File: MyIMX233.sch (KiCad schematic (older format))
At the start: 40 parts, among them IC1 iMX233, IC2 DDR_SDRAM_MT46_x16, J1 USB_A, J2 Micro_SD_Card, SW1 SWITCH_PUSHBUTTON, Y1 24Mhz

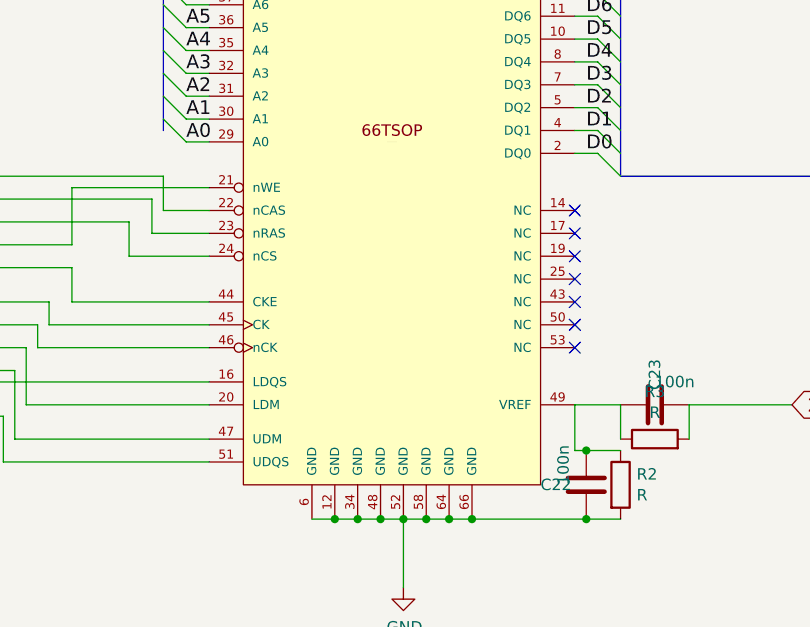
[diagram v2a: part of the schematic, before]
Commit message: refs added plus tuned lengths of d8..15 and addr
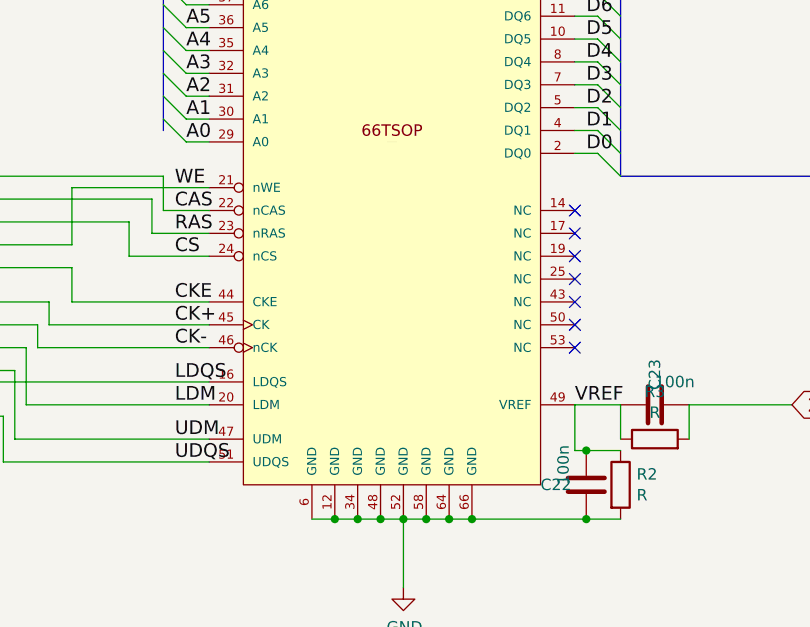
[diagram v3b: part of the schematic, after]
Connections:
- net CK+: now reaches IC1.36 (EMI_CLK), IC2.45 (CK)
- net CK-: now reaches IC1.37 (EMI_CLKn), IC2.46 (nCK)
- net LDQS: now reaches IC1.39 (EMI_DQS0), IC2.16 (LDQS)
- net UDQS: now reaches IC1.40 (EMI_DQS1), IC2.51 (UDQS)
- net LDM: now reaches IC1.46 (EMI_DQM0), IC2.20 (LDM)
- net UDM: now reaches IC1.56 (EMI_DQM1), IC2.47 (UDM)
- net CAS: now reaches IC1.61 (EMI_CASn), IC2.22 (nCAS)
- net RAS: now reaches IC1.62 (EMI_RASn), IC2.23 (nRAS)
- net CS: now reaches IC1.63 (EMI_CE0n), IC2.24 (nCS)
- net WE: now reaches IC1.77 (EMI_WEn), IC2.21 (nWE)
- net CKE: now reaches IC1.78 (EMI_CKE), IC2.44 (CKE)
- net VREF: now reaches C22.2, C23.1, IC2.49 (VREF), R2.1, R3.1
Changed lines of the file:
@@
 Wire Wire Line
 	2800 6800 2500 6800
+Text Label 10550 5550 0    60   ~ 0
+VREF
+Text Label 8800 4600 0    60   ~ 0
+WE
+Text Label 8800 4700 0    60   ~ 0
+CAS
+Text Label 8800 4800 0    60   ~ 0
+RAS
+Text Label 8800 4900 0    60   ~ 0
+CS
+Text Label 8800 5100 0    60   ~ 0
+CKE
+Text Label 8800 5200 0    60   ~ 0
+CK+
+Text Label 8800 5300 0    60   ~ 0
+CK-
+Text Label 8800 5450 0    60   ~ 0
+LDQS
+Text Label 8800 5550 0    60   ~ 0
+LDM
+Text Label 8800 5700 0    60   ~ 0
+UDM
+Text Label 8800 5800 0    60   ~ 0
+UDQS
 $EndSCHEMATC

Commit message: updated pcb export with 3d step files plus my new DDR step and FreeCAD proj
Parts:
- J1: footprint Connectors:USB_Micro-B -> mylib:USB_Micro-B_MOLEX_105017-0001
- J2: footprint Connectors_Hirose:microSD_Card_Receptacle_Hirose_DM3AT-SF-PEJM5 -> mylib:microSD_Card_Receptacle_Hirose_DM3AT-SF-PEJM5
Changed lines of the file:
@@
 F 0 "J1" H 1805 4117 50  0000 C CNN
 F 1 "USB_A" H 1805 4026 50  0000 C CNN
-F 2 "Connectors:USB_Micro-B" H 1900 3600 50  0001 C CNN
+F 2 "mylib:USB_Micro-B_MOLEX_105017-0001" H 1900 3600 50  0001 C CNN
 F 3 "" H 1900 3600 50  0001 C CNN
 	1    1750 3650
@@
 F 0 "J2" H 1700 9217 50  0000 C CNN
 F 1 "Micro_SD_Card" H 1700 9126 50  0000 C CNN
-F 2 "Connectors_Hirose:microSD_Card_Receptacle_Hirose_DM3AT-SF-PEJM5" H 2900 8800 50  0001 C CNN
+F 2 "mylib:microSD_Card_Receptacle_Hirose_DM3AT-SF-PEJM5" H 2900 8800 50  0001 C CNN
 F 3 "" H 1750 8500 50  0001 C CNN
 	1    1750 8500

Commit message: before dcdc
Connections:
- net SD_CMD: now reaches IC1.83 (SSP1_CMD-JTAG_TDO), J2.3 (CMD)
- net SD0: now reaches IC1.84 (SSP1_DATA0-JTAG_TDI), J2.7 (DAT0)
- net SD1: now reaches IC1.85 (SSP1_DATA1-I2C_SCL-JTAG_TCLK), J2.8 (DAT1)
- net SD2: now reaches IC1.86 (SSP1_DATA2-I2C_SDA-JTAG_RTCK), J2.1 (DAT2)
- net SD3: now reaches IC1.87 (SSP1_DATA3-JTAG_TMS), J2.2 (DAT3/CD)
- net SD_CLK: now reaches IC1.90 (SSP1_SCK-JTAG_TRST), J2.5 (CLK)
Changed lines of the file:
@@
 	2950 8200 2650 8200
-Wire Wire Line
-	3250 8400 3250 8450
-Wire Wire Line
-	3250 8450 2800 8450
-Wire Wire Line
-	2800 8450 2800 8300
 Wire Wire Line
 	2800 8300 2650 8300
@@
 Text Label 8800 5800 0    60   ~ 0
 UDQS
+Wire Wire Line
+	3250 8425 2800 8425
+Wire Wire Line
+	2800 8425 2800 8300
+Wire Wire Line
+	3250 8425 3250 8400
+Text Label 3125 8100 0    60   ~ 0
+SD0
+Text Label 3150 8200 0    60   ~ 0
+SD1
+Text Label 2675 8200 0    60   ~ 0
+SD2
+Text Label 3175 8425 0    60   ~ 0
+SD3
+Text Label 3100 8600 0    60   ~ 0
+SD_CLK
+Text Label 3175 8000 0    60   ~ 0
+SD_CMD
 $EndSCHEMATC

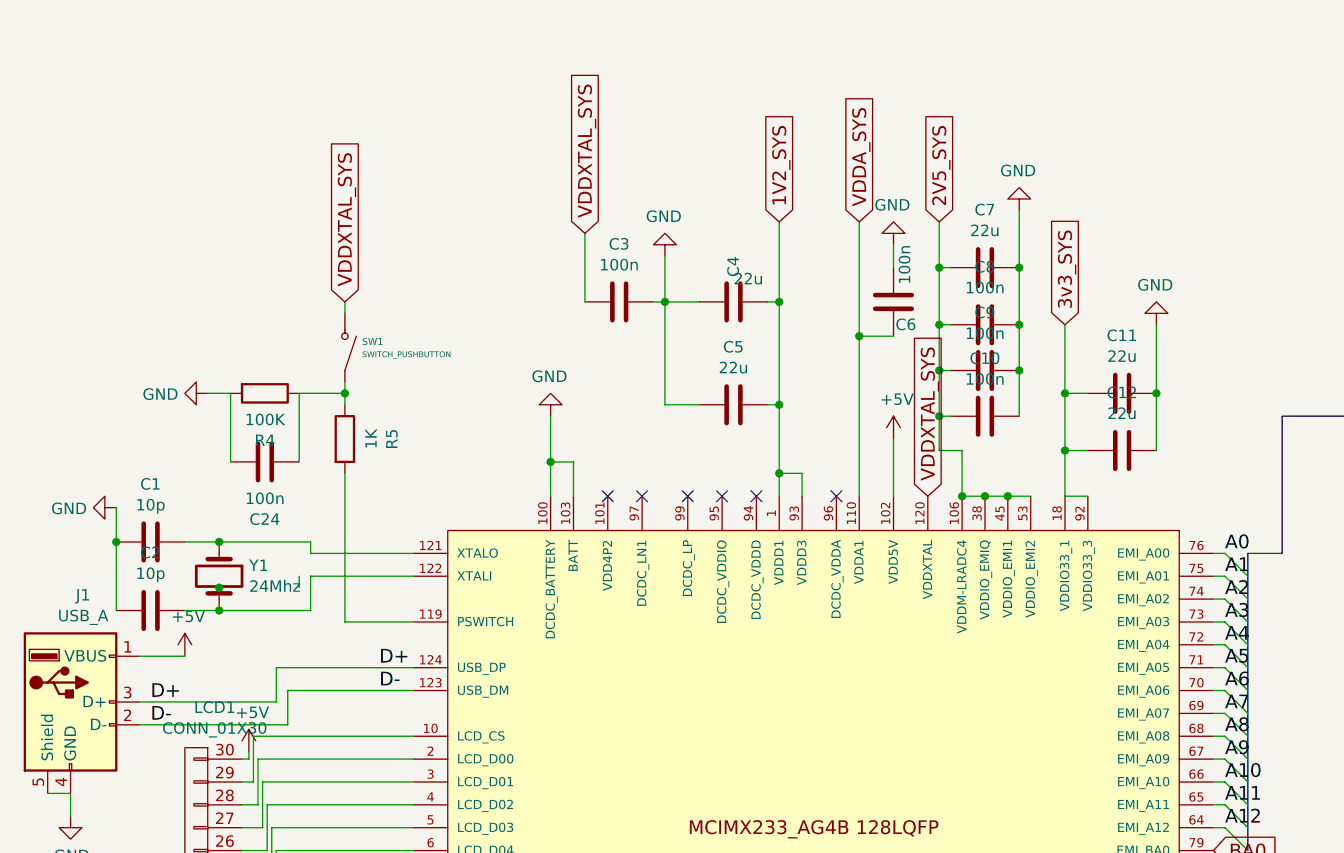
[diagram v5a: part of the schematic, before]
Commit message: updated with step files new battery and inductor diag
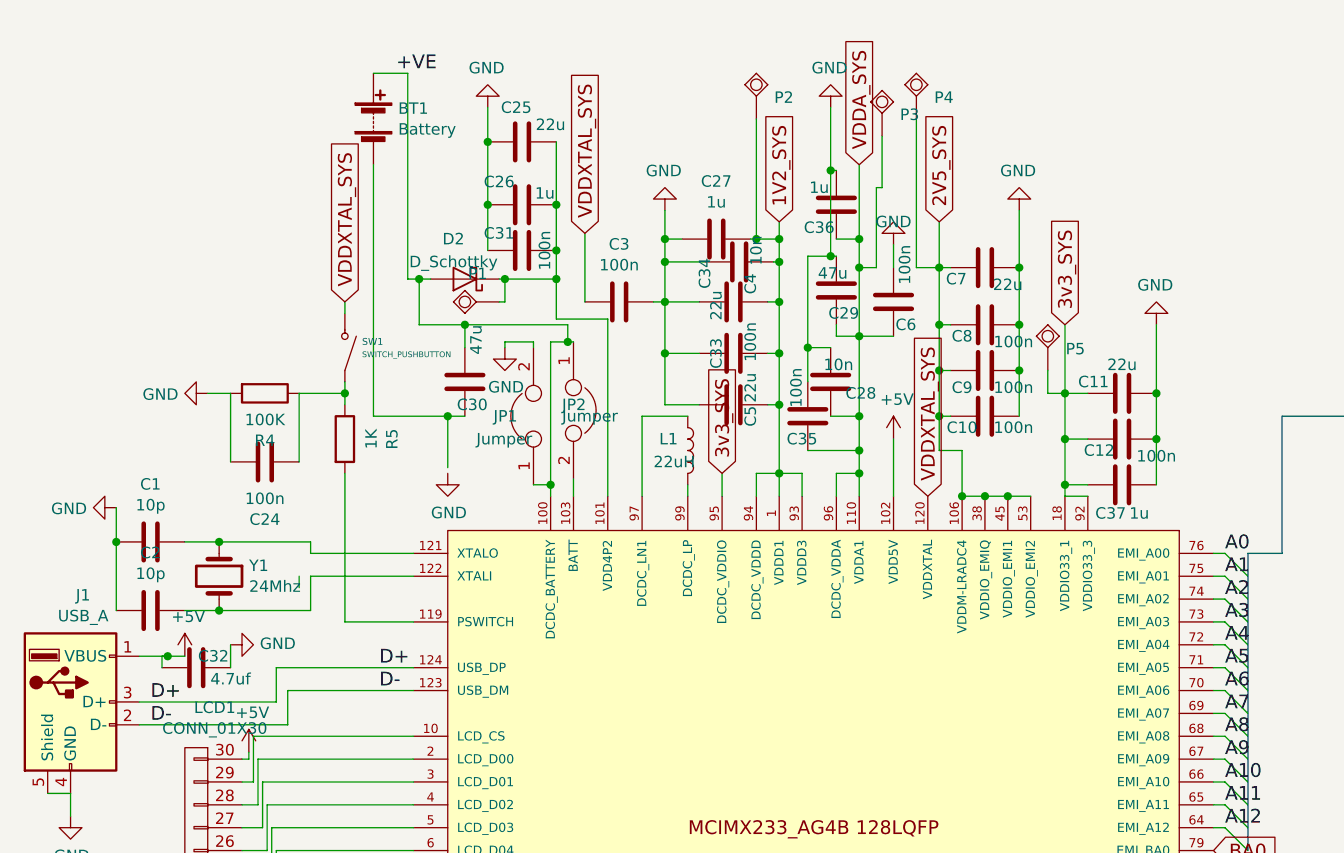
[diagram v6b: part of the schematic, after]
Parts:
- added BT1: Battery, Connectors_JST:JST_XH_B02B-XH-A_02x2.50mm_Straight, symbol Battery
- added C25: 22u, Capacitors_SMD:C_0805_HandSoldering, symbol C
- added C26, C27: 1u, Capacitors_SMD:C_0402, symbol C
- added C28, C34: 10n, Capacitors_SMD:C_0402, symbol C
- added C29, C30: 47u, Capacitors_SMD:C_0805_HandSoldering, symbol C
- added C31, C33, C35: 100n, Capacitors_SMD:C_0402, symbol C
- added C32: 4.7uf, Capacitors_SMD:C_0603_HandSoldering, symbol C
- added C36, C37: 1u, Capacitors_SMD:C_0603_HandSoldering, symbol C
- added D2: D_Schottky, Diodes_SMD:D_SOD-323_HandSoldering, symbol D_Schottky
- added JP1, JP2: Jumper, Pin_Headers:Pin_Header_Straight_1x02_Pitch2.54mm, symbol Jumper
- added L1: 22uH, mylib:Bourns22uh6x6mm, symbol L
- added P1: P4v2, iMX233-OLinuXino-NANO_Rev_B:GOGO_TESTPAD40_OBLONG, symbol GOGO_TESTPAD
- added P2: 1v2, iMX233-OLinuXino-NANO_Rev_B:GOGO_TESTPAD40_OBLONG, symbol GOGO_TESTPAD
- added P3: VDDA1v8, iMX233-OLinuXino-NANO_Rev_B:GOGO_TESTPAD40_OBLONG, symbol GOGO_TESTPAD
- added P4: 2v5, iMX233-OLinuXino-NANO_Rev_B:GOGO_TESTPAD40_OBLONG, symbol GOGO_TESTPAD
- added P5: 3v3, iMX233-OLinuXino-NANO_Rev_B:GOGO_TESTPAD40_OBLONG, symbol GOGO_TESTPAD
- C12: value 22u -> 100n
- C13: footprint Capacitors_SMD:C_0603 -> Capacitors_SMD:C_0603_HandSoldering
- IC2: footprint opendous:TSOP66_JEDEC_DDR_SDRAM -> mylib:TSOP66_JEDEC_DDR_SDRAM
- J1: footprint mylib:USB_Micro-B_MOLEX_105017-0001 -> conn-fci:CONN-10118194-0001LF-FCI
- R1, R4, R5: footprint Resistors_SMD:R_0603 -> Resistors_SMD:R_0603_HandSoldering
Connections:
- net +5V: now also C32.1
- net 1V2_SYS: now also IC1.94 (DCDC_VDDD), C27.2, C33.1, C34.1, P2.P$1 (PP)
- net 2V5_SYS: now also P4.P$1 (PP)
- net 3v3_SYS: now also IC1.95 (DCDC_VDDIO), C37.1, P5.P$1 (PP)
- net GND: now also C25.1, C26.1, C27.1, C28.1, C29.1, C31.2, C32.2, C33.2, C34.2, C35.1, C36.1, C37.2, JP1.2; no longer IC1.100 (DCDC_BATTERY), IC1.103 (BATT)
- net VDDA_SYS: now also IC1.96 (DCDC_VDDA), C28.2, C29.2, C35.2, C36.2, P3.P$1 (PP)
- net at IC1.101 (VDD4P2): now also C25.2, C26.2, C31.1, D2.1 (K), P1.P$1 (PP)
- net at IC1.97 (DCDC_LN1): now also L1.1
- net at IC1.99 (DCDC_LP): now also L1.2
- new net: IC1.103 (BATT), JP2.2
- new net: BT1.2 (-), C30.2
- new net +VE: BT1.1 (+), C30.1, D2.2 (A), IC1.100 (DCDC_BATTERY), JP1.1, JP2.1
- no-connect marks 28 -> 22
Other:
- moved on the sheet: C12

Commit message: pcb-1.0
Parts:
- added C39: 100n, Capacitors_SMD:C_0402, symbol C
- added C40: 10n, Capacitors_SMD:C_0402, symbol C
- added D3: LED, LEDs:LED_0603, symbol LED
- added R6: 10k, Resistors_SMD:R_0603_HandSoldering, symbol R
- added R7: 1k, Resistors_SMD:R_0603_HandSoldering, symbol R
- C12: footprint Capacitors_SMD:C_0805_HandSoldering -> Capacitors_SMD:C_0402
- P1, P2, P3, P4, P5: footprint iMX233-OLinuXino-NANO_Rev_B:GOGO_TESTPAD40_OBLONG -> iMX233-OLinuXino-NANO_Rev_BEagle:GOGO_TESTPAD2
- R1: value R -> 1k
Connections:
- net +5V: now also I2C1.1 (P1)
- net 3v3_SYS: now also C39.2, C40.2
- net GND: now also BT1.2 (-), C30.2, C39.1, C40.1, D3.1 (K), R6.1; no longer J1.4 (GND)
- net at IC1.89 (DEBUG): now also DEBUG_UART1.1 (P1)
- net at IC1.91 (PWM2-GPMI_RDY3): now also R7.2
- new net: J1.4 (GND), R6.2
- new net: D3.2 (A), R7.1
- no-connect marks 22 -> 18
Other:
- moved on the sheet: C28, C29, C35, C36, C6

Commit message: 2nd version
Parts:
- added D? (x2): 5.1v, symbol D_Zener
- added J?: USB_OTG, symbol USB_OTG
- R2, R3: value R -> 1K1%
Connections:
- net +5V: now also D?.1 (K)
- net GND: now also D?.2 (A), D?.2 (A), J?.5 (GND), J?.6 (Shield)
- net at R1.1: no longer IC1.88 (SSP1_DETECT-GPMI_CE3N-USB_ID)
- new net USB_ID: D?.1 (K), IC1.88 (SSP1_DETECT-GPMI_CE3N-USB_ID), J?.4 (ID)
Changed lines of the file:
@@
 LIBS:valves
 LIBS:iMX233-OLinuXino-NANO_Rev_B
-LIBS:opendous
-LIBS:conn-fci
 LIBS:MyIMX233-cache
 EELAYER 26 0
@@
 P 10750 5900
 F 0 "R2" H 10820 5946 50  0000 L CNN
-F 1 "R" H 10820 5855 50  0000 L CNN
+F 1 "1K1%" H 10820 5855 50  0000 L CNN
 F 2 "Resistors_SMD:R_0603" V 10680 5900 50  0001 C CNN
 F 3 "" H 10750 5900 50  0001 C CNN
@@
 P 10900 5700
 F 0 "R3" V 11107 5700 50  0000 C CNN
-F 1 "R" V 11016 5700 50  0000 C CNN
+F 1 "1K1%" V 11016 5700 50  0000 C CNN
 F 2 "Resistors_SMD:R_0603" V 10830 5700 50  0001 C CNN
 F 3 "" H 10900 5700 50  0001 C CNN
@@
 Connection ~ 5300 9050
 Wire Wire Line
-	3250 8500 3200 8500
-Wire Wire Line
-	3200 8500 3200 9150
-Wire Wire Line
 	3200 9450 3200 9500
 Wire Wire Line
@@
 Wire Wire Line
 	2550 7850 2450 7850
+$Comp
+L D_Zener D?
+U 1 1 598B134C
+P 1250 3600
+F 0 "D?" V 1204 3679 50  0000 L CNN
+F 1 "5.1v" V 1295 3679 50  0000 L CNN
+F 2 "" H 1250 3600 50  0001 C CNN
+F 3 "" H 1250 3600 50  0001 C CNN
+	1    1250 3600
+	0    1    1    0
+$EndComp
+$Comp
+L +5V #PWR?
+U 1 1 598B5CE8
+P 1250 3400
+F 0 "#PWR?" H 1250 3250 50  0001 C CNN
+F 1 "+5V" H 1265 3573 50  0000 C CNN
+F 2 "" H 1250 3400 50  0001 C CNN
+F 3 "" H 1250 3400 50  0001 C CNN
+	1    1250 3400
+	1    0    0    -1
+$EndComp
+$Comp
+L GND #PWR?
+U 1 1 598B5D7D
+P 1250 3850
+F 0 "#PWR?" H 1250 3600 50  0001 C CNN
+F 1 "GND" H 1255 3677 50  0000 C CNN
+F 2 "" H 1250 3850 50  0001 C CNN
+F 3 "" H 1250 3850 50  0001 C CNN
+	1    1250 3850
+	1    0    0    -1
+$EndComp
+Wire Wire Line
+	1250 3750 1250 3850
+Wire Wire Line
+	1250 3450 1250 3400
+$Comp
+L USB_OTG J?
+U 1 1 598B7260
+P 1200 4650
+F 0 "J?" H 1255 5117 50  0000 C CNN
+F 1 "USB_OTG" H 1255 5026 50  0000 C CNN
+F 2 "" H 1350 4600 50  0001 C CNN
+F 3 "" H 1350 4600 50  0001 C CNN
+	1    1200 4650
+	1    0    0    -1
+$EndComp
+Text GLabel 3250 8500 3    60   Input ~ 0
+USB_ID
+Text GLabel 1500 4850 2    60   Input ~ 0
+USB_ID
+$Comp
+L D_Zener D?
+U 1 1 598BC40A
+P 1500 5100
+F 0 "D?" V 1454 5179 50  0000 L CNN
+F 1 "5.1v" V 1545 5179 50  0000 L CNN
+F 2 "" H 1500 5100 50  0001 C CNN
+F 3 "" H 1500 5100 50  0001 C CNN
+	1    1500 5100
+	0    1    1    0
+$EndComp
+$Comp
+L GND #PWR?
+U 1 1 598BC5E8
+P 1500 5350
+F 0 "#PWR?" H 1500 5100 50  0001 C CNN
+F 1 "GND" H 1505 5177 50  0000 C CNN
+F 2 "" H 1500 5350 50  0001 C CNN
+F 3 "" H 1500 5350 50  0001 C CNN
+	1    1500 5350
+	1    0    0    -1
+$EndComp
+Wire Wire Line
+	1500 5350 1500 5250
+Wire Wire Line
+	1500 4950 1500 4850
+$Comp
+L GND #PWR?
+U 1 1 598BCAA4
+P 1200 5150
+F 0 "#PWR?" H 1200 4900 50  0001 C CNN
+F 1 "GND" H 1205 4977 50  0000 C CNN
+F 2 "" H 1200 5150 50  0001 C CNN
+F 3 "" H 1200 5150 50  0001 C CNN
+	1    1200 5150
+	1    0    0    -1
+$EndComp
+Wire Wire Line
+	1200 5150 1200 5050
+Wire Wire Line
+	1100 5050 1100 5100
+Wire Wire Line
+	1100 5100 1200 5100
+Connection ~ 1200 5100
 $EndSCHEMATC
